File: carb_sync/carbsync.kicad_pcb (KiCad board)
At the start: 2 copper layers, 73.1 x 126.3 mm, 49 parts, among them IC1 ATMEGA328P-A, P1 CONN_02X03, P2 CONN_01X02, SW1 SPST, SW2 SPST, SW3 SPST, SW4 SPST, U1 MPXV6115V, U2 MPXV6115V, U3 MPXV6115V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

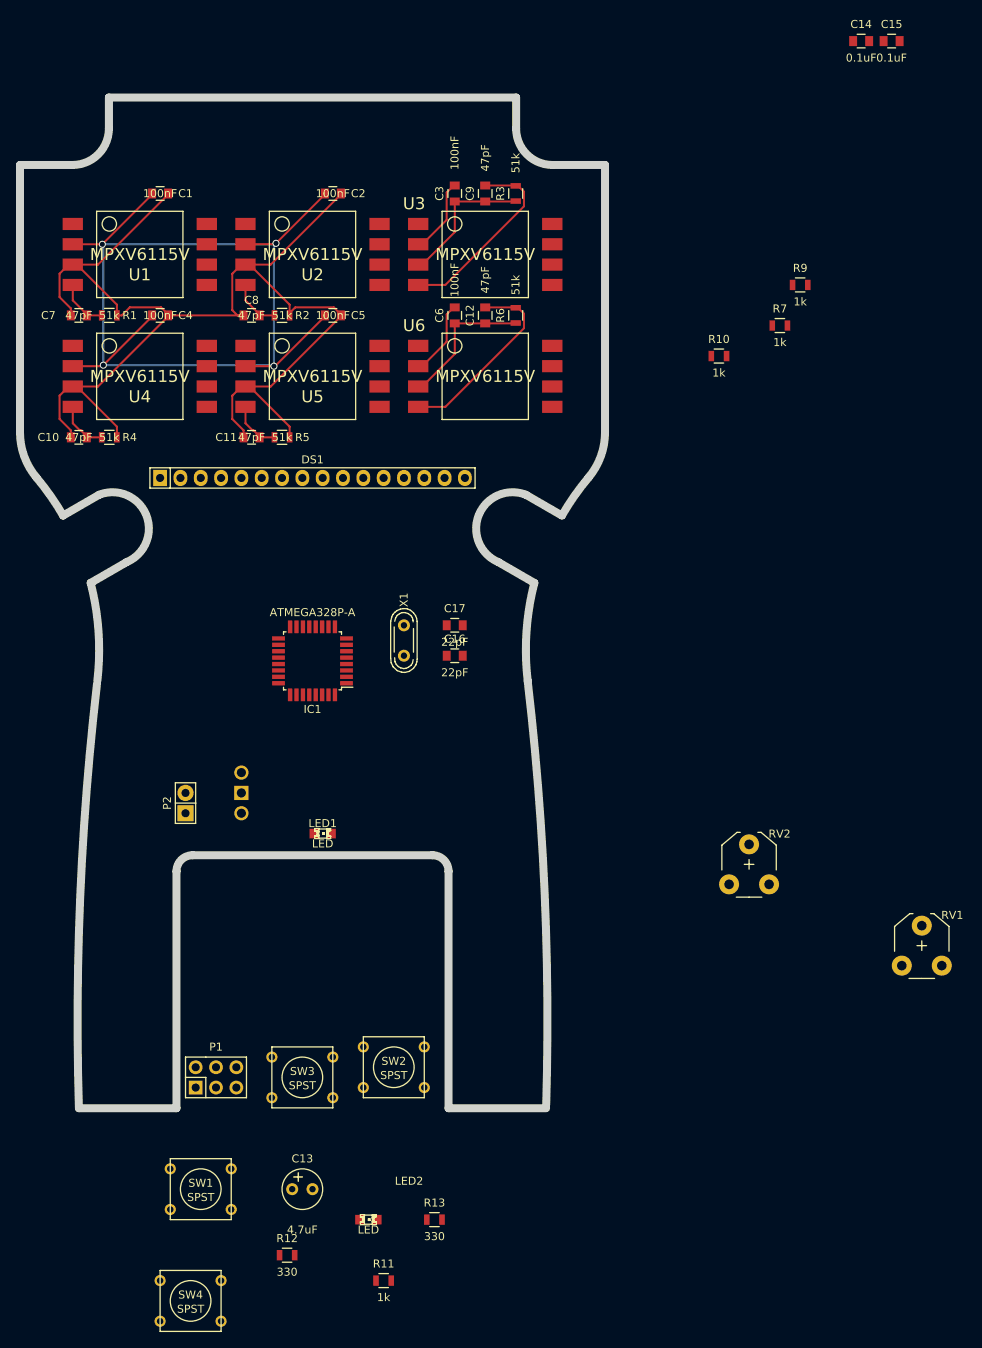
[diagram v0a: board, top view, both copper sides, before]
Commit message: [carb_sync] Initial complete layout. LCD connector to pads.
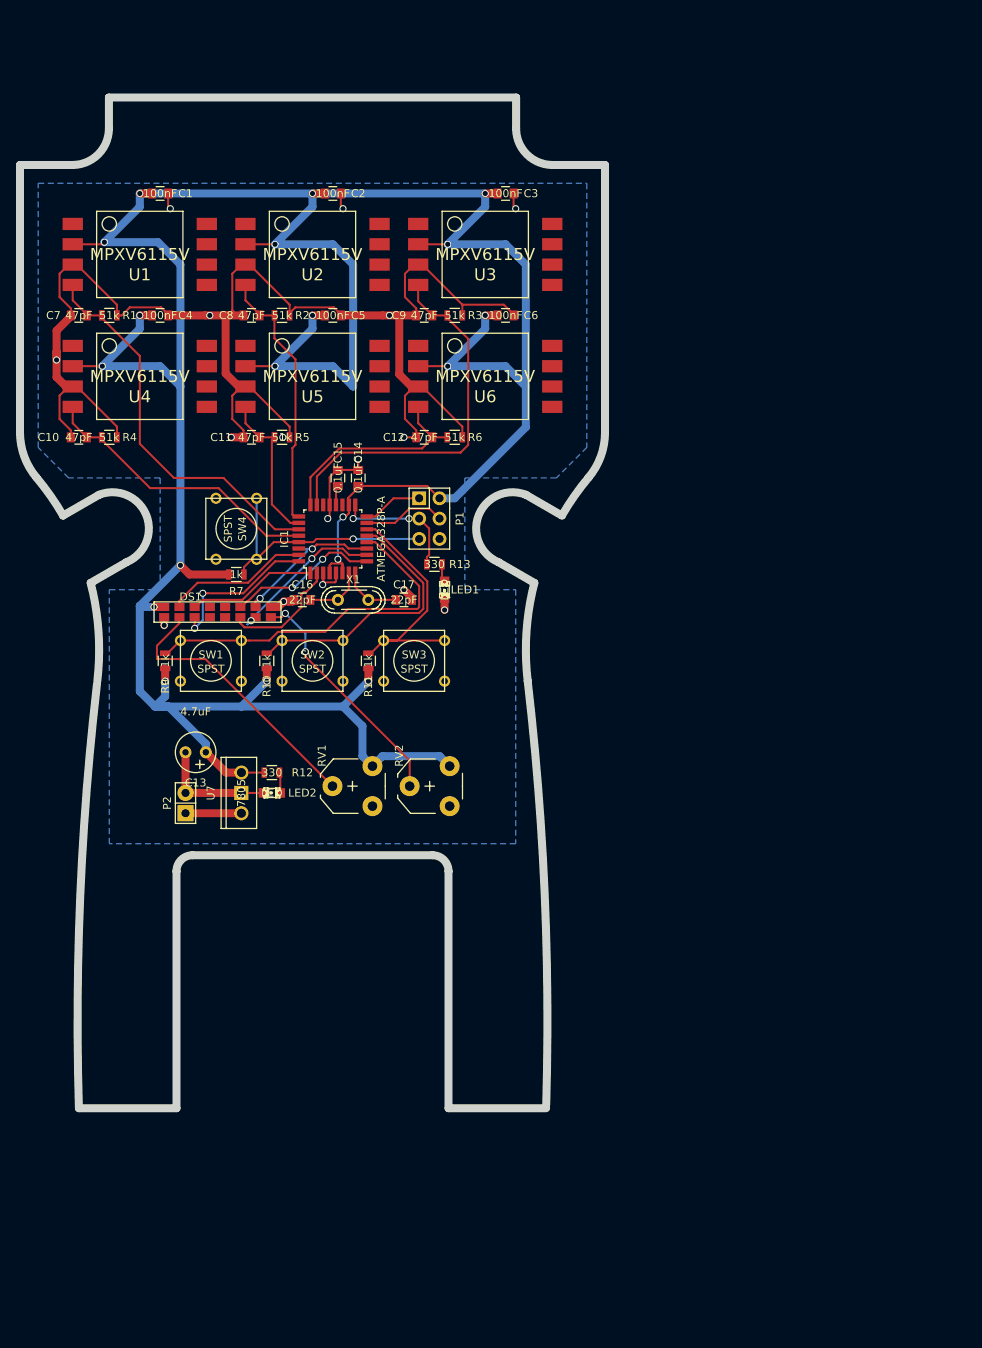
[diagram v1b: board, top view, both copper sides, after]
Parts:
- DS1: footprint Pin_Headers:Pin_Header_Straight_1x16 -> Connect:GS_8x2
- U7: moved to F.Cu
- moved SW4 96.7 mm to (122.6, 80.0), turned to 270 degrees
- moved R9 92.2 mm to (113.7, 96.5), turned to 270 degrees
- moved C15 88.2 mm to (135.3, 73.7), turned to 90 degrees
- moved C14 83.3 mm to (137.8, 73.7), turned to 90 degrees
- moved R13 81.9 mm to (147.3, 84.5), turned to 180 degrees
- moved R11 77.5 mm to (139.1, 96.5), turned to 270 degrees
- moved P1 74.8 mm to (146.7, 78.7), turned to 270 degrees
- moved R7 74.7 mm to (122.6, 85.7), turned to 180 degrees
- moved RV1 69.1 mm to (139.6, 114.7), turned to 90 degrees
- moved R10 68.2 mm to (126.4, 96.5), turned to 270 degrees
- moved SW1 66.1 mm to (119.4, 96.5)
- moved R12 60.4 mm to (127.0, 110.5), turned to 180 degrees
- moved C13 55.7 mm to (118.7, 108.0), turned to 180 degrees
- moved LED2 54.7 mm to (127.0, 113.0), turned to 180 degrees
- moved SW3 53.9 mm to (144.8, 96.5)
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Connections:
- C10 pad 1: S4 -> S6
- C11 pad 1: S5 -> S4
- C12 pad 1: S6 -> S2
- C7 pad 1: S1 -> S5
- C8 pad 1: S2 -> S3
- C9 pad 1: S3 -> S1
- R1 pad 1: S1 -> S5
- R12 pad 2: Net-(R12-Pad2) -> +5V
- R2 pad 1: S2 -> S3
- R3 pad 1: S3 -> S1
- R4 pad 1: S4 -> S6
- R5 pad 1: S5 -> S4
- R6 pad 1: S6 -> S2
- U1 pad 4: S1 -> S5
- U2 pad 4: S2 -> S3
- U3 pad 4: S3 -> S1
- U4 pad 4: S4 -> S6
- U5 pad 4: S5 -> S4
- U6 pad 4: S6 -> S2
- U7 pad VO: Net-(R12-Pad2) -> +5V
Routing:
- net +5V: track 148.1 -> 418.5 mm, vias 4 -> 19
- net B0: track 0.00 -> 45.6 mm
- net S5: track 6.47 -> 48.8 mm
- net S1: track 6.52 -> 48.0 mm
- net GND: track 190.2 -> 225.4 mm, vias 0 -> 16
- net Net-(DS1-Pad3): track 0.00 -> 34.9 mm
- net B1: track 0.00 -> 34.6 mm
- net /RESET: track 0.00 -> 31.9 mm, vias 0 -> 1
- net B2: track 0.00 -> 31.1 mm
- net Net-(DS1-Pad15): track 0.00 -> 30.0 mm, vias 0 -> 2
- net S2: track 6.40 -> 27.4 mm
- net LCD_DB6: track 0.00 -> 20.0 mm, vias 0 -> 2
- net LCD_RW: track 0.00 -> 19.9 mm, vias 0 -> 2
- net LCD_DB5: track 0.00 -> 19.1 mm, vias 0 -> 2
- net LCD_RS: track 0.00 -> 18.1 mm
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- added copper zone on B.Cu, net GND
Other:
- net class Power added: clearance 0.254, trace_width 1, via_dia 0.889, via_drill 0.635

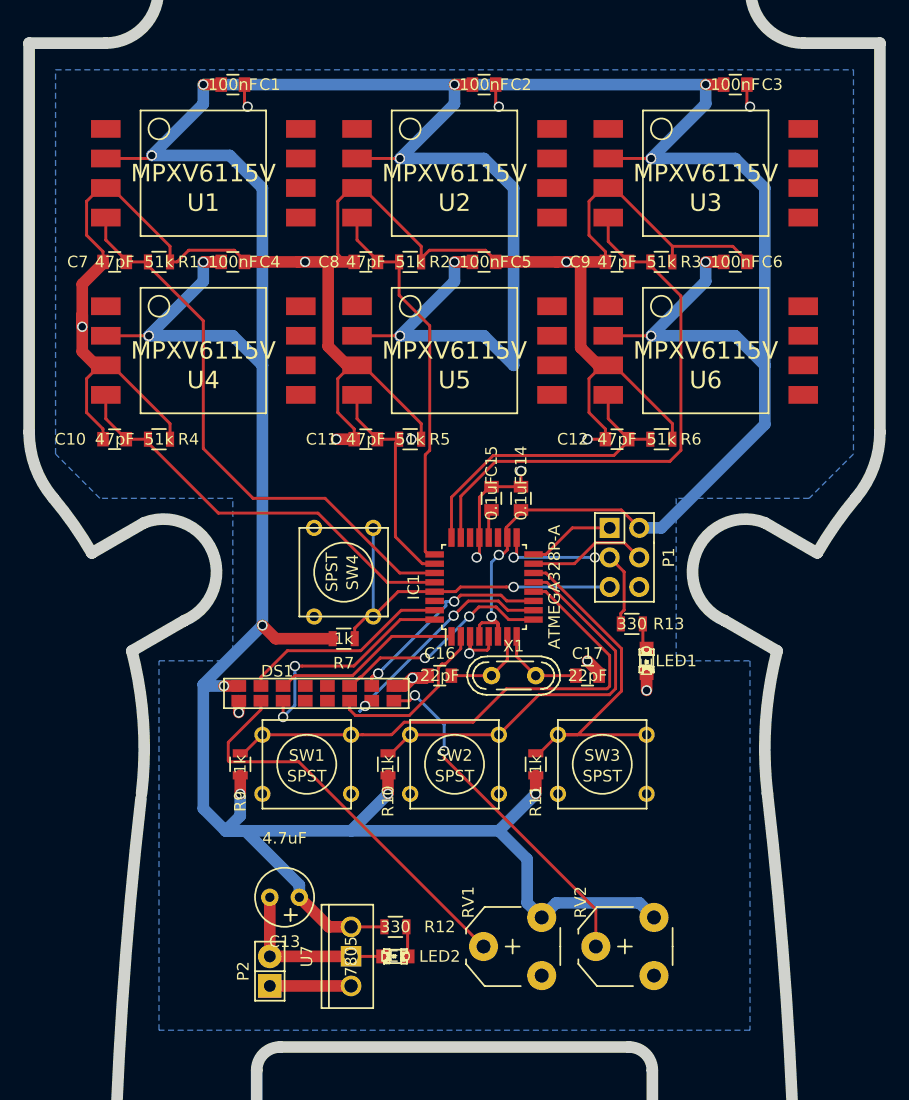
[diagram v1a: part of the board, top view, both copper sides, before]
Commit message: [carb_sync] Changed crystal footprint for ATMEGA328P.
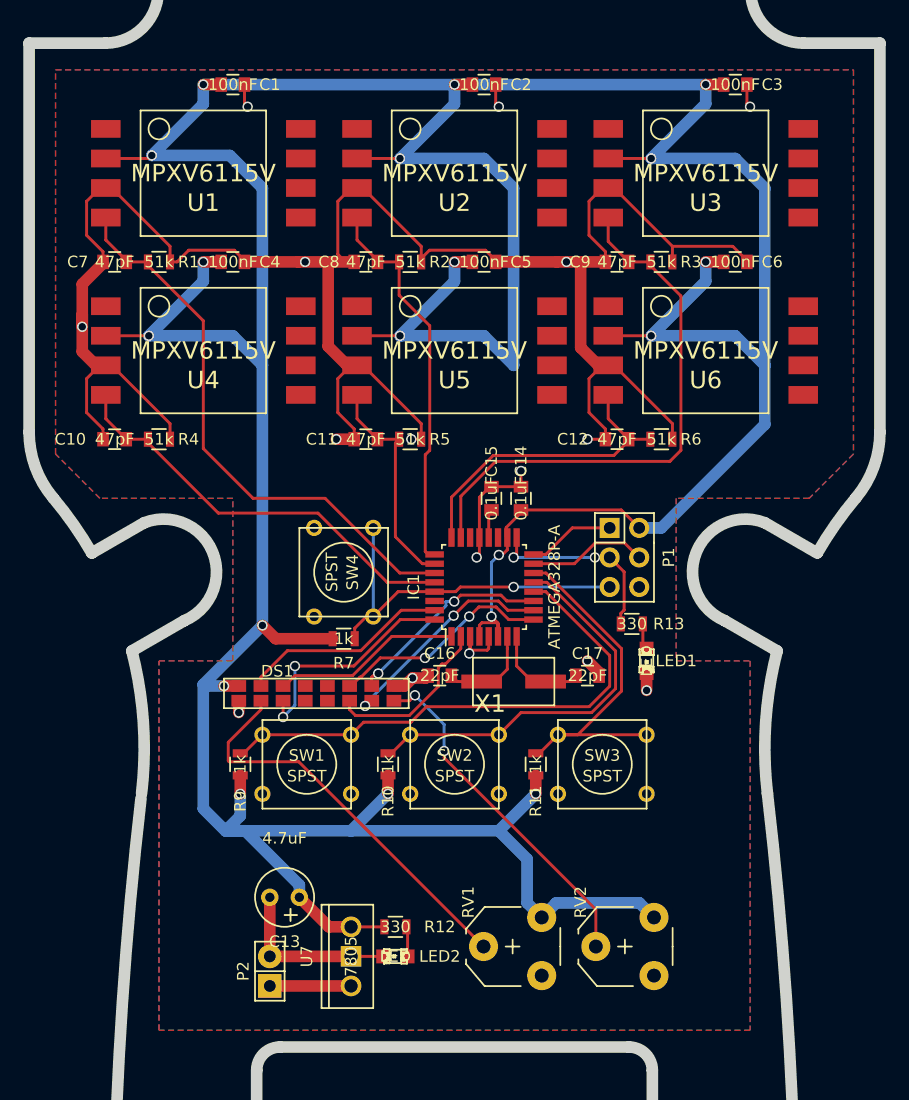
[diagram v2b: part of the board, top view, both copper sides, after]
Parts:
- X1: footprint Crystals:Crystal_HC52-U_Vertical -> NQBit:HC-49USX_SMD
- moved X1 0.51 mm to (137.2, 89.4), turned to 0 degrees
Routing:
- net Net-(C16-Pad2): track 7.38 -> 8.28 mm
- net Net-(C17-Pad2): track 7.50 -> 8.39 mm
- net LCD_DB6: track 20.0 -> 19.4 mm
- added copper zone on F.Cu, net GND
